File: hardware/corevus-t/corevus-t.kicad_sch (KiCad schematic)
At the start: 50 parts, among them J1 MF3, J10 pinheader, J2 XH, J3 MF3, J4 XH, J5 XH, J6 XH, J7 XH, J8 pinheader, J9 XH, Q2 NMOS, Q3 AO3401A, Q32 AO3400, SW3 BOOT, SW3 RST, U1 LIS2DE12, U2 TPS54302, U3 STM32G431KBU3, U4 TMC2209-LA, Y1 12 MHz

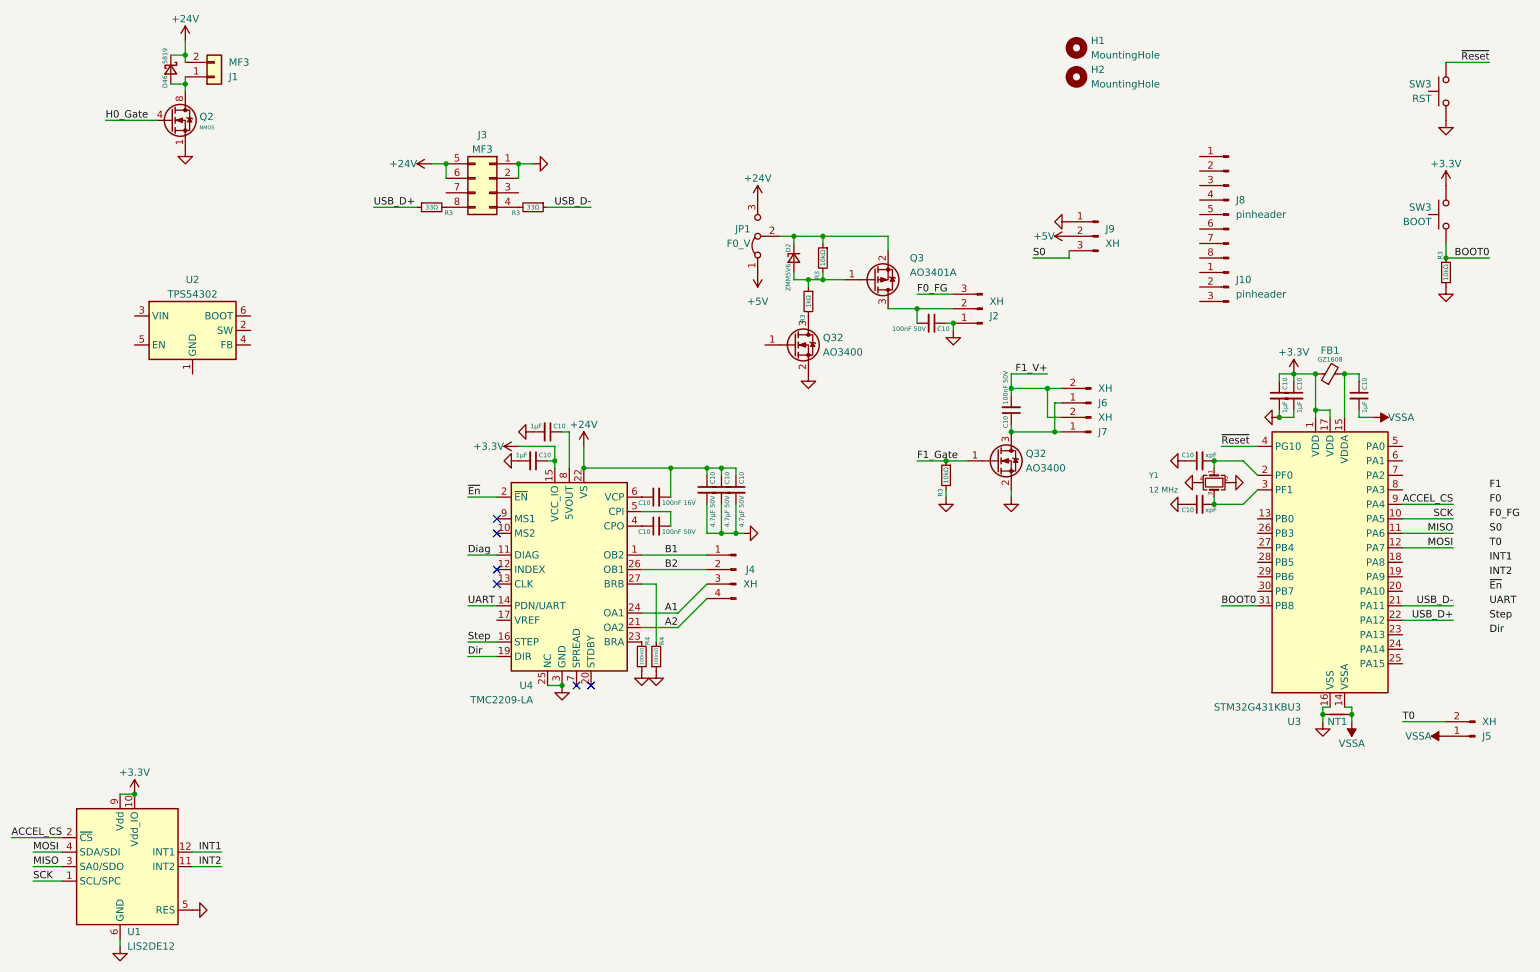
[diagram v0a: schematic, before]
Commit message: v0.4 mostly complete, board needs minor revisions (e.g. pin swap)
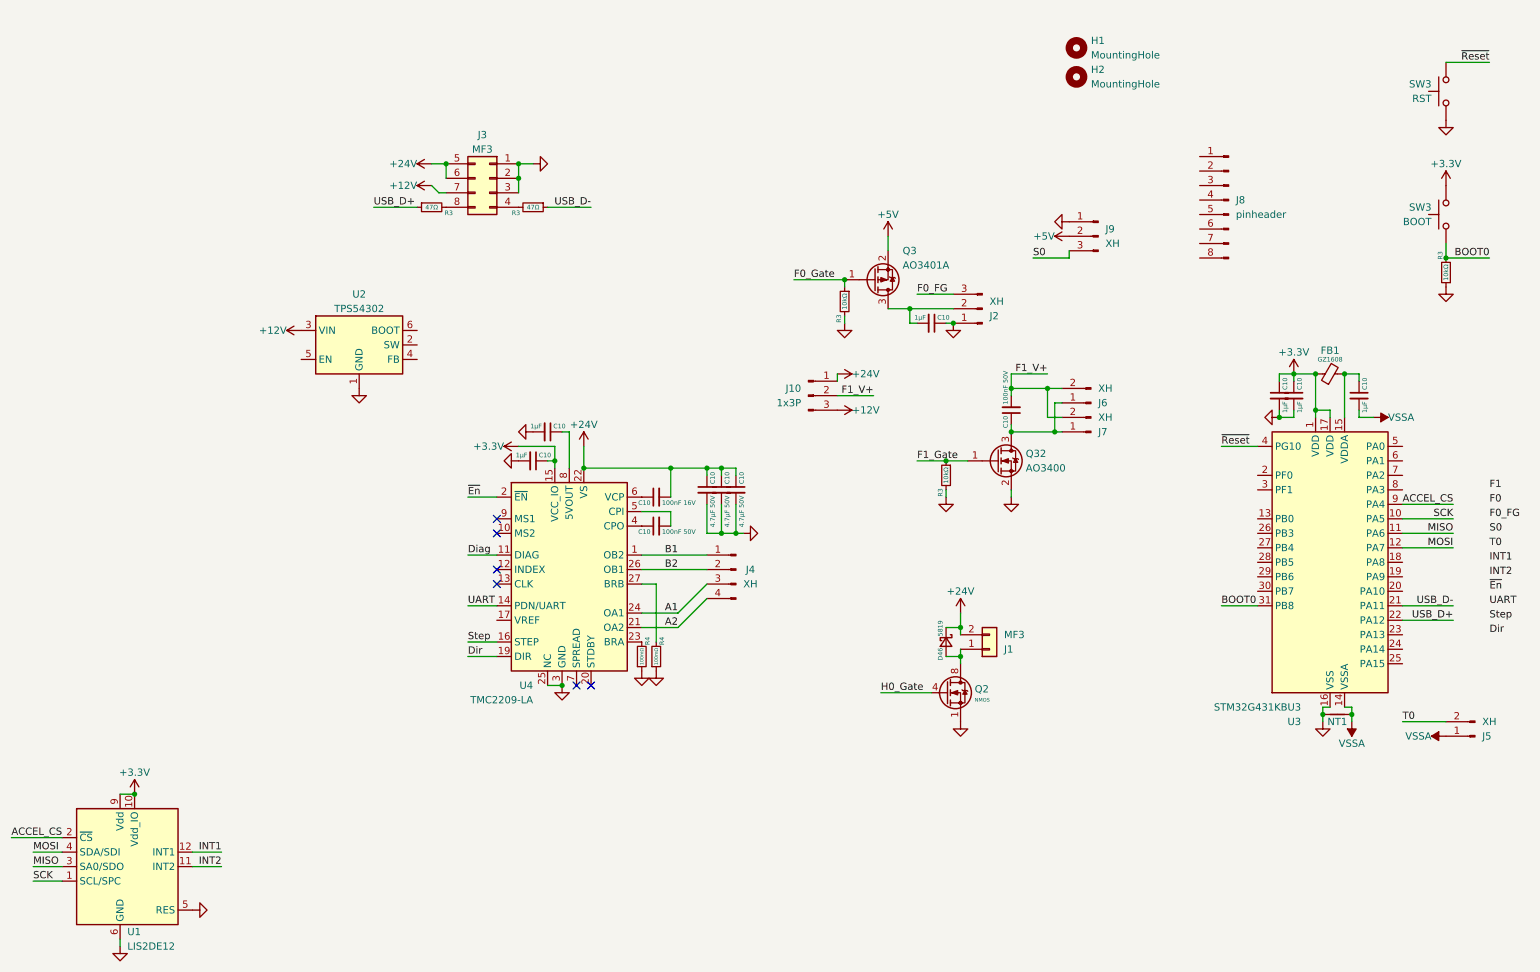
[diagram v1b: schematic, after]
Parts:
- removed C10 (x2): xpF, AlphaLib:0402C, symbol Device:C_Small
- removed D2: ZMM5V6, symbol Device:D_Zener_Small
- removed JP1: F0_V, Jumper:SolderJumper-3_P1.3mm_Bridged12_RoundedPad1.0x1.5mm, symbol Jumper:Jumper_3_Bridged12
- removed Q32: AO3400, Package_TO_SOT_SMD:SOT-23, symbol Device:Q_NMOS_GSD
- removed R3: 1kΩ, AlphaLib:0402R, symbol Device:R_Small
- removed R3: 10kΩ, AlphaLib:0402R, symbol Device:R_Small
- removed Y1: 12 MHz, Crystal:Crystal_SMD_3225-4Pin_3.2x2.5mm, symbol Device:Crystal_GND24_Small
- added R3: 10kΩ, AlphaLib:0402R, symbol Device:R_Small
- C10: value 100nF 50V -> 1μF
- J10: value pinheader -> 1x3P
- R3: value 33Ω -> 47Ω
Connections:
- net +24V: now also J10.1 (Pin_1)
- net +5V: now also Q3.2 (S)
- net F1_V+: now also J10.2 (Pin_2)
- net GND: now also J3.3 (Pin_3), U2.1 (GND), R3.2
- net F0_Gate: now reaches Q3.1 (G)
- net F0_Gate: now also R3.1
- net +12V: now reaches U2.3 (VIN)
- net +12V: now also J10.3 (Pin_3), J3.7 (Pin_7)
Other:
- moved on the sheet: D46, J1, J10, Q2, U2
